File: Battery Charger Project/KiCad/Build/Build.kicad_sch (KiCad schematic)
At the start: 25 parts, among them J1 Screw_Terminal_01x03, J10 726386-2, J2 Screw_Terminal_01x03, J3 Screw_Terminal_01x02, J5 726386-2, J6 726386-2, J7 726386-2, J9 726386-2, U1 LAUNCHXL-F28379D, U3 MCS1801GS-25-P

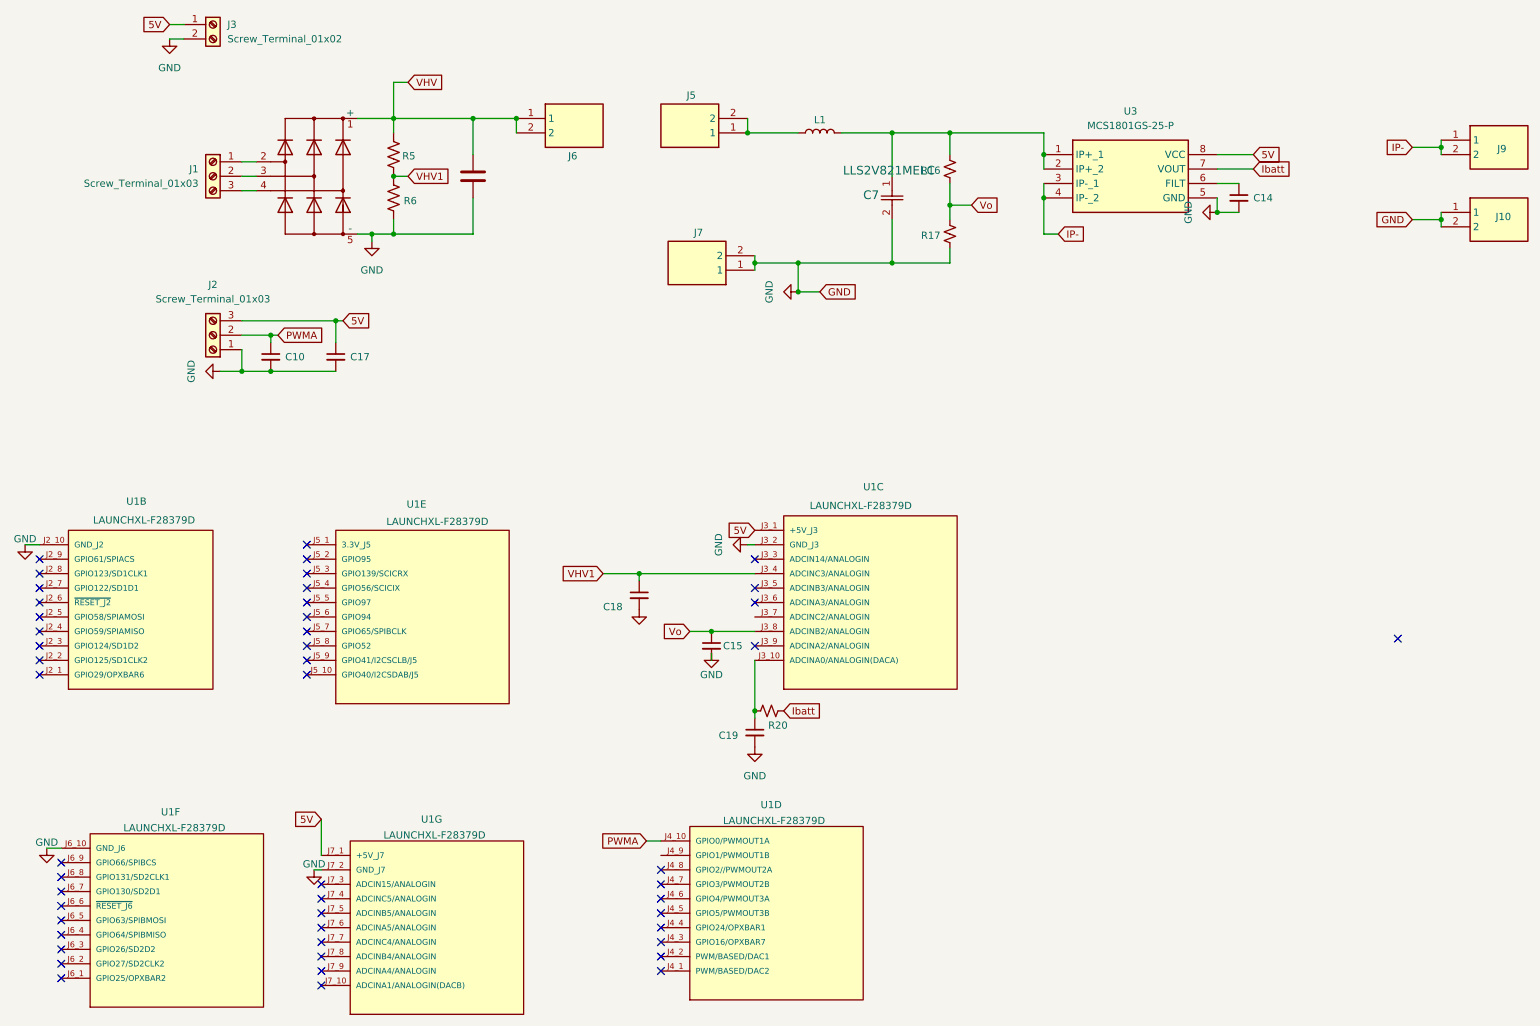
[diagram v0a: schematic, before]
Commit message: Made more progress on schematic
Changed current sense IC.
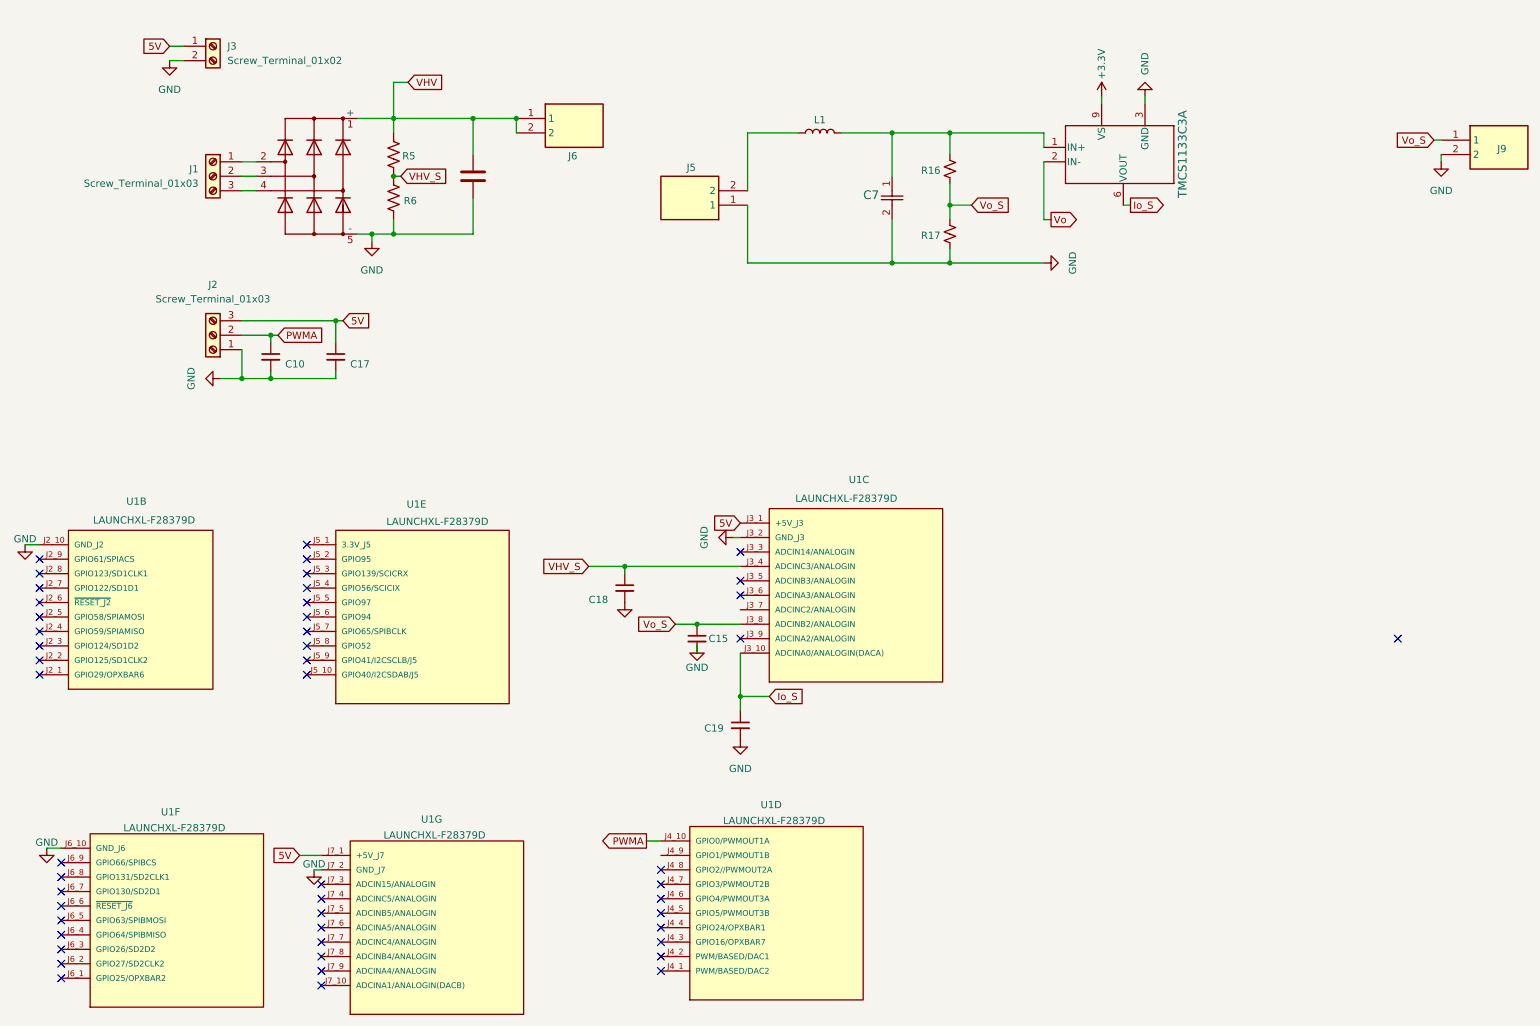
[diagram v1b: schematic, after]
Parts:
- removed C14: C_Small, Capacitor_SMD:C_0805_2012Metric_Pad1.18x1.45mm_HandSolder, symbol Device:C_Small
- removed J10, J7: 726386-2, KiCad:726386-2, symbol mouseric:726386-2
- removed R20: R_Small_US, Resistor_SMD:R_1206_3216Metric, symbol Device:R_Small_US
- removed U3: MCS1801GS-25-P, KiCadCS:SOIC127P600X175-8N, symbol MCS1801GS-25-P:MCS1801GS-25-P
- added U2: TMCS1133C3A, DVG0010A_PMCS1133A1AQDVGR_TEX, symbol Wind symbols:PMCS1133A1AQDVGR
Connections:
- net GND: now also J5.1, J9.2, U2.3 (GND)
- net Vo: now also U2.2 (IN-); no longer C15.1, R16.2, R17.1, U1.J3_8 (ADCINB2/ANALOGIN)
- net Io_S: now reaches C19.1, U1.J3_10 (ADCINA0/ANALOGIN(DACA))
- net Io_S: now also U2.6 (VOUT)
- net at J5.2, L1.1: no longer J5.1
- net at C7.1, L1.2, R16.1: now also U2.1 (IN+)
- net IP- renamed Vo_S
- net Vo_S: now also C15.1, R16.2, R17.1, U1.J3_8 (ADCINB2/ANALOGIN); no longer J9.2
- net VHV1 renamed VHV_S
- new net +3.3V: U2.9 (VS)
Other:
- moved on the sheet: C15, C18, C19, J3, J5, U1C

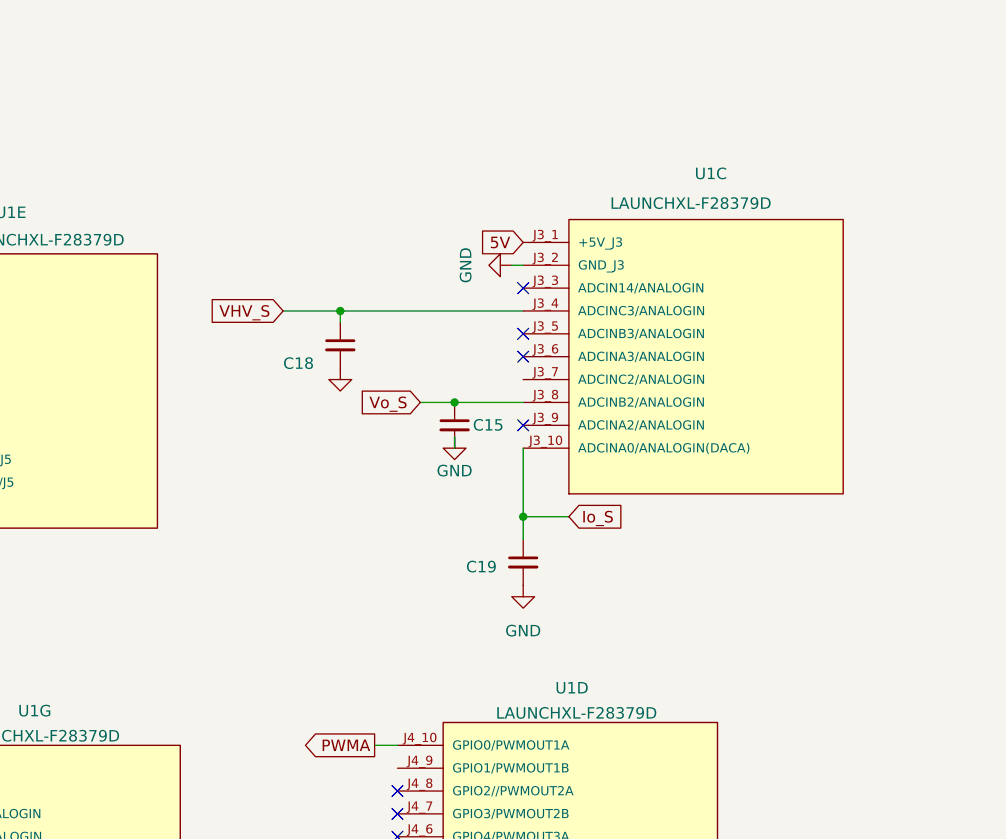
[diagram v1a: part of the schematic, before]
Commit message: Added demo folder
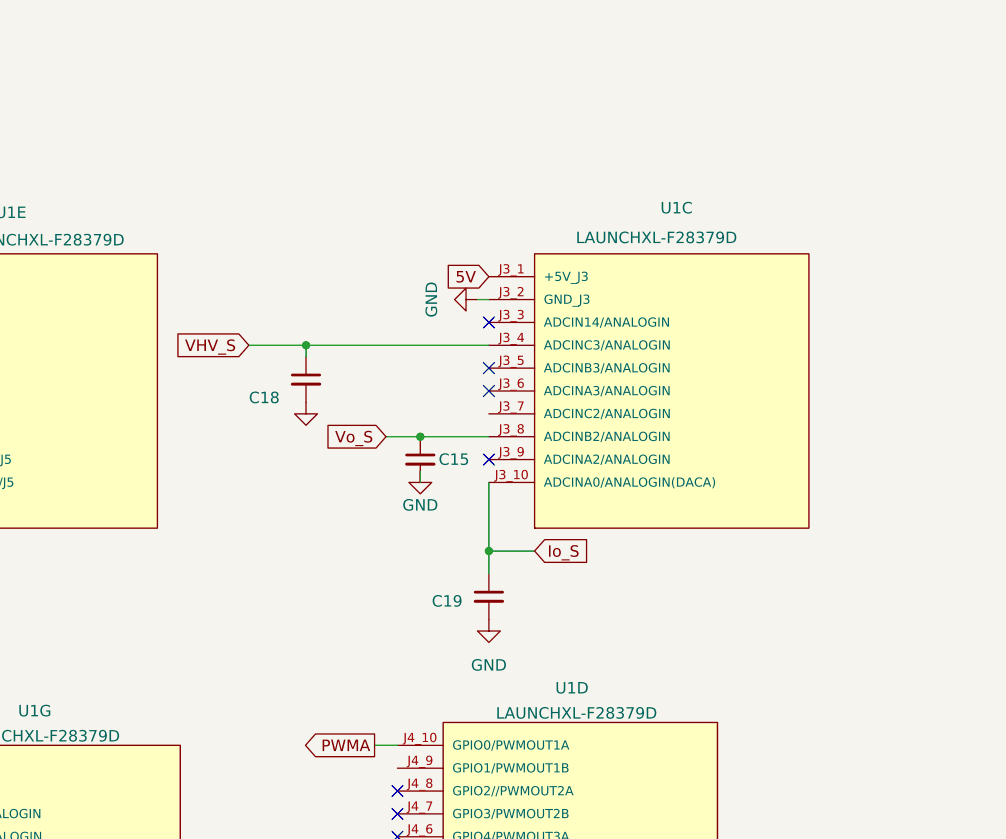
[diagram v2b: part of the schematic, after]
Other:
- moved on the sheet: C15, C18, C19, U1C
